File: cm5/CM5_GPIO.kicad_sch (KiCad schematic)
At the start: 24 parts, among them J14 JST_SHBM04B-SRSS-TB, J3 Conn_01x03, J6 Conn_02x03_Counter_Clockwise, U2 TLV320ADC6120IRTER, U5 74LVC1G07SE-7

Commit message: Ordered v2 PCB
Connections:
- net GND: now also J6.2 (Pin_2), J6.5 (Pin_5); no longer J6.3 (Pin_3), J6.4 (Pin_4)
- net at J6.1 (Pin_1): now also U2.3 (IN2P_GPI1); no longer U2.2 (IN1M)
- net at U2.1 (IN1P): now also J6.6 (Pin_6); no longer J6.2 (Pin_2)
- net at U2.4 (IN2M_GPO1): now also J6.4 (Pin_4); no longer J6.5 (Pin_5)
- new net: J6.3 (Pin_3), U2.2 (IN1M)

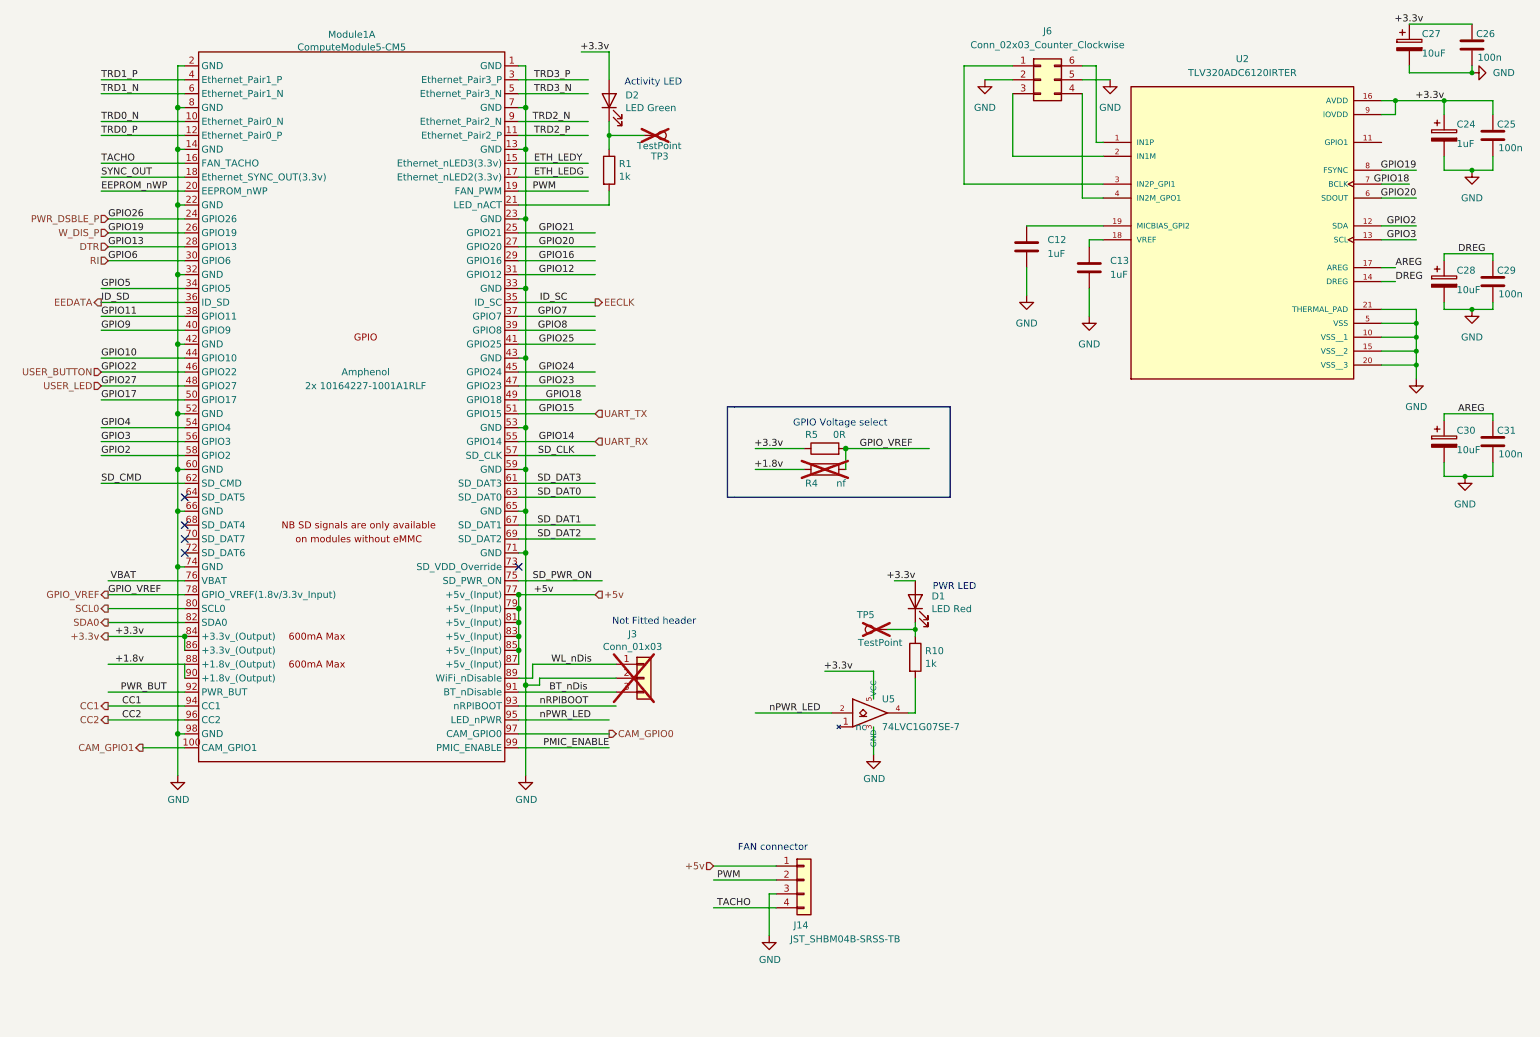
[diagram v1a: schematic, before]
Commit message: PCM1863 switchover (#5)
* Oops, basically brand new ADC design using a new chip

* Working PCB and working driver, sort of

* --amend
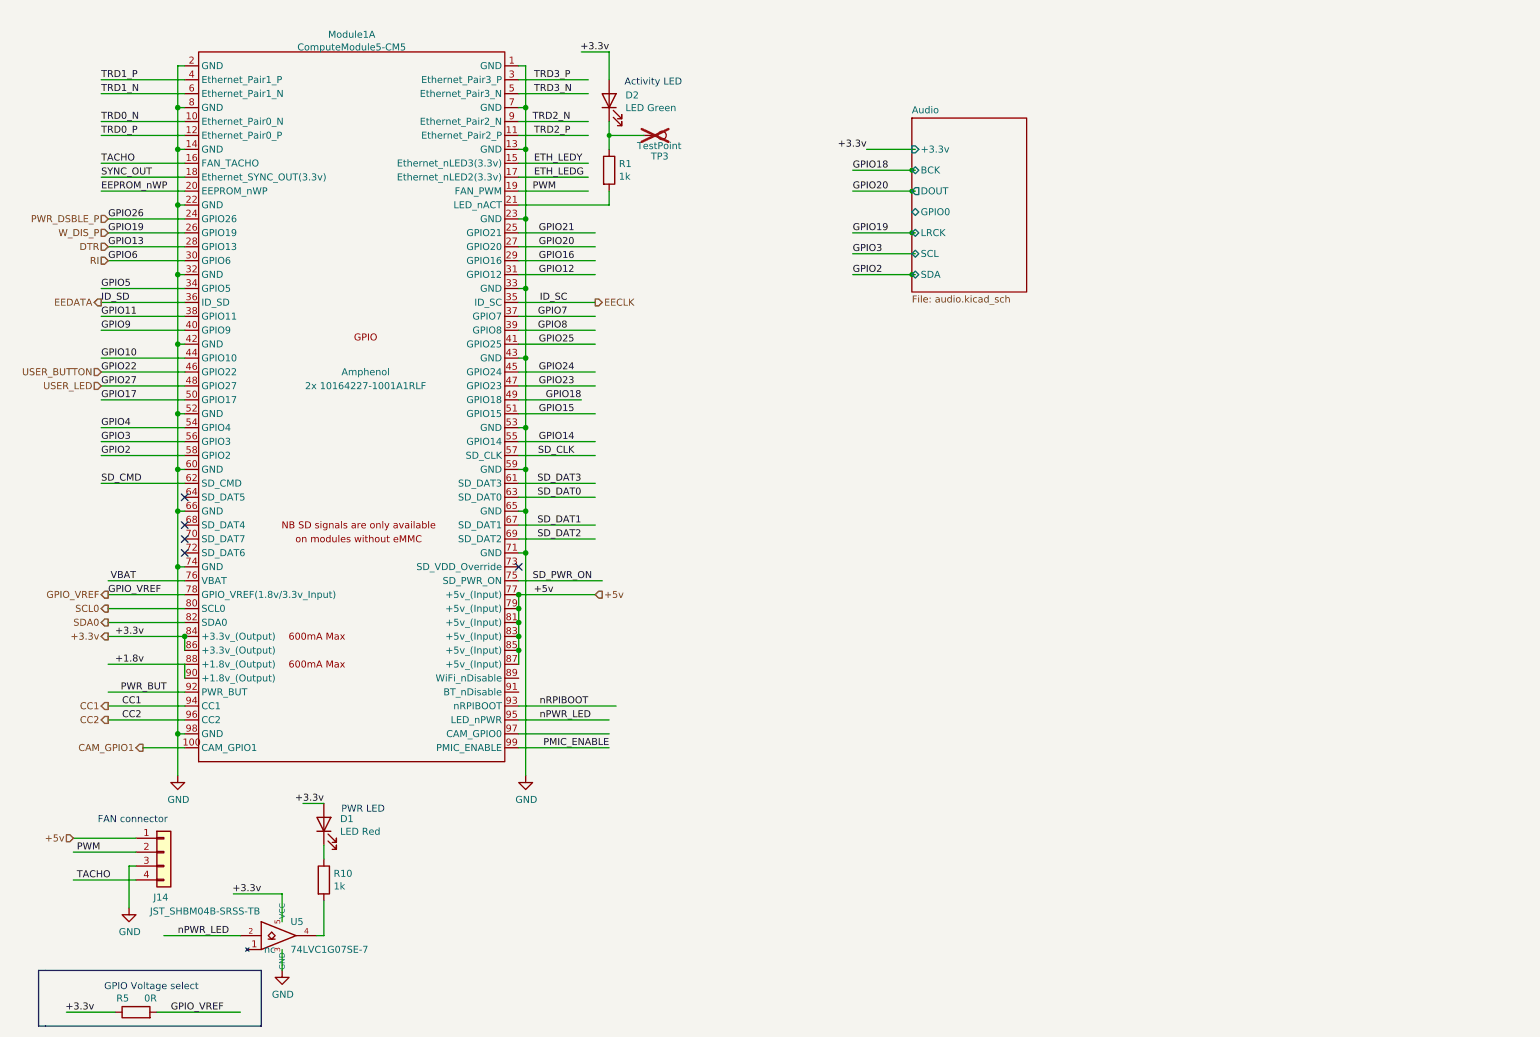
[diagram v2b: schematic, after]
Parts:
- removed C12, C13: 1uF, digikey-footprints:0603, symbol Device:C
- removed C24: 1uF, digikey-footprints:0805, symbol Device:C_Polarized
- removed C25, C26, C29, C31: 100n, Capacitor_SMD:C_0402_1005Metric, symbol Device:C
- removed C27, C28, C30: 10uF, Capacitor_SMD:CP_Elec_6.3x5.9, symbol Device:C_Polarized
- removed J3: Conn_01x03, Connector_PinHeader_2.54mm:PinHeader_1x03_P2.54mm_Vertical, symbol Connector_Generic:Conn_01x03
- removed J6: Conn_02x03_Counter_Clockwise, Connector_PinHeader_2.54mm:PinHeader_2x03_P2.54mm_Vertical, symbol Connector_Generic:Conn_02x03_Counter_Clockwise
- removed R4: nf, Resistor_SMD:R_0805_2012Metric_Pad1.20x1.40mm_HandSolder, symbol Device:R
- removed TP5: TestPoint, TestPoint:TestPoint_Pad_2.0x2.0mm, symbol Connector:TestPoint
- removed U2: TLV320ADC6120IRTER, TLV320ADC6120IRTER:IC_TLV320ADC6120IRTER, symbol TLV320ADC6120IRTER:TLV320ADC6120IRTER
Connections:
- net BT_nDis: no longer names the net of Module1.91 (BT_nDisable)
- net CAM_GPIO0: no longer names the net of Module1.97 (CAM_GPIO0)
- net UART_RX renamed GPIO14
- net UART_TX renamed GPIO15
- net WL_nDis: no longer names the net of Module1.89 (WiFi_nDisable)
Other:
- added sheet Audio (audio.kicad_sch)
- note removed: "Not Fitted header"
- moved on the sheet: D1, J14, R10, R5, U5

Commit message: Getting started on StudioHub adapter
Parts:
- added J5: RJ45_Hanrun_HR911105A_Horizontal, Connector_RJ:RJ45_Hanrun_HR911105A_Horizontal, symbol Connector:RJ45_Hanrun_HR911105A_Horizontal
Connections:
- net ETH_LEDG: now also J5.9
- net ETH_LEDY: now also J5.12
- net GND: now also J5.10, J5.11
- net TRD0_N: now also J5.2 (TD-)
- net TRD0_P: now also J5.1 (TD+)
- net TRD1_N: now also J5.6 (RD-)
- net TRD1_P: now also J5.3 (RD+)
